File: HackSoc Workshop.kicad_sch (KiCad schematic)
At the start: 35 parts, among them J1 USB_B_Micro, J2 ISP, SW1 SW_Push, SW2 SW_Push, SW3 SW_Push, SW4 SW_Push, SW5 SW_Push, SW6 SW_Push, SW7 SW_Push, U1 ATmega32U4-M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

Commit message: update
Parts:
- SW1, SW2, SW3, SW4, SW5, SW6, SW7: footprint Button_Switch_THT:SW_PUSH_6mm_H8.5mm -> Footprints:SW_TS-1187A-B-A-B
- Y1: footprint Crystal:Crystal_SMD_7050-4Pin_7.0x5.0mm -> Crystal:Crystal_SMD_3225-4Pin_3.2x2.5mm
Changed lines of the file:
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@@
     (property "Reference" "SW1" (id 0) (at 69.215 42.545 0))
     (property "Value" "SW_Push" (id 1) (at 69.215 40.005 0))
-    (property "Footprint" "Button_Switch_THT:SW_PUSH_6mm_H8.5mm" (id 2) (at 69.215 33.655 0)
+    (property "Footprint" "Footprints:SW_TS-1187A-B-A-B" (id 2) (at 69.215 33.655 0)
       (effects (font (size 1.27 1.27)) hide)
     )
@@
     (property "Reference" "SW3" (id 0) (at 117.475 100.965 0))
     (property "Value" "SW_Push" (id 1) (at 132.715 100.965 0))
-    (property "Footprint" "Button_Switch_THT:SW_PUSH_6mm_H8.5mm" (id 2) (at 122.555 97.155 0)
+    (property "Footprint" "Footprints:SW_TS-1187A-B-A-B" (id 2) (at 122.555 97.155 0)
       (effects (font (size 1.27 1.27)) hide)
     )
@@
     (property "Reference" "SW6" (id 0) (at 117.475 108.585 0))
     (property "Value" "SW_Push" (id 1) (at 132.715 108.585 0))
-    (property "Footprint" "Button_Switch_THT:SW_PUSH_6mm_H8.5mm" (id 2) (at 122.555 104.775 0)
+    (property "Footprint" "Footprints:SW_TS-1187A-B-A-B" (id 2) (at 122.555 104.775 0)
       (effects (font (size 1.27 1.27)) hide)
     )
@@
     (property "Reference" "SW2" (id 0) (at 117.475 98.425 0))
     (property "Value" "SW_Push" (id 1) (at 132.715 98.425 0))
-    (property "Footprint" "Button_Switch_THT:SW_PUSH_6mm_H8.5mm" (id 2) (at 122.555 94.615 0)
+    (property "Footprint" "Footprints:SW_TS-1187A-B-A-B" (id 2) (at 122.555 94.615 0)
       (effects (font (size 1.27 1.27)) hide)
     )
@@
     (property "Reference" "SW4" (id 0) (at 117.475 103.505 0))
     (property "Value" "SW_Push" (id 1) (at 132.715 103.505 0))
-    (property "Footprint" "Button_Switch_THT:SW_PUSH_6mm_H8.5mm" (id 2) (at 122.555 99.695 0)
+    (property "Footprint" "Footprints:SW_TS-1187A-B-A-B" (id 2) (at 122.555 99.695 0)
       (effects (font (size 1.27 1.27)) hide)
     )
@@
     (property "Reference" "SW7" (id 0) (at 117.475 111.125 0))
     (property "Value" "SW_Push" (id 1) (at 132.715 111.125 0))
-    (property "Footprint" "Button_Switch_THT:SW_PUSH_6mm_H8.5mm" (id 2) (at 122.555 107.315 0)
+    (property "Footprint" "Footprints:SW_TS-1187A-B-A-B" (id 2) (at 122.555 107.315 0)
       (effects (font (size 1.27 1.27)) hide)
     )
@@
     (property "Reference" "Y1" (id 0) (at 36.195 36.2798 0))
     (property "Value" "12MHz" (id 1) (at 36.195 38.8167 0))
-    (property "Footprint" "Crystal:Crystal_SMD_7050-4Pin_7.0x5.0mm" (id 2) (at 36.195 42.545 0)
+    (property "Footprint" "Crystal:Crystal_SMD_3225-4Pin_3.2x2.5mm" (id 2) (at 36.195 42.545 0)
       (effects (font (size 1.27 1.27)) hide)
     )
@@
     (property "Reference" "SW5" (id 0) (at 117.475 106.045 0))
     (property "Value" "SW_Push" (id 1) (at 132.715 106.045 0))
-    (property "Footprint" "Button_Switch_THT:SW_PUSH_6mm_H8.5mm" (id 2) (at 122.555 102.235 0)
+    (property "Footprint" "Footprints:SW_TS-1187A-B-A-B" (id 2) (at 122.555 102.235 0)
       (effects (font (size 1.27 1.27)) hide)
     )
@@
     )
     (path "/00000000-0000-0000-0000-0000609bc448"
-      (reference "SW1") (unit 1) (value "SW_Push") (footprint "Button_Switch_THT:SW_PUSH_6mm_H8.5mm")
+      (reference "SW1") (unit 1) (value "SW_Push") (footprint "Footprints:SW_TS-1187A-B-A-B")
     )
     (path "/a5cf3bdf-9580-4a89-9b38-de8f920e3709"
-      (reference "SW2") (unit 1) (value "SW_Push") (footprint "Button_Switch_THT:SW_PUSH_6mm_H8.5mm")
+      (reference "SW2") (unit 1) (value "SW_Push") (footprint "Footprints:SW_TS-1187A-B-A-B")
     )
     (path "/1c2ae23d-1cd7-4546-aa49-900e7a3c7475"
-      (reference "SW3") (unit 1) (value "SW_Push") (footprint "Button_Switch_THT:SW_PUSH_6mm_H8.5mm")
+      (reference "SW3") (unit 1) (value "SW_Push") (footprint "Footprints:SW_TS-1187A-B-A-B")
     )
     (path "/e7470108-55db-4f72-aba2-dd70fe36ad14"
-      (reference "SW4") (unit 1) (value "SW_Push") (footprint "Button_Switch_THT:SW_PUSH_6mm_H8.5mm")
+      (reference "SW4") (unit 1) (value "SW_Push") (footprint "Footprints:SW_TS-1187A-B-A-B")
     )
     (path "/fd588f97-a508-46a8-ad7f-2d03d16e0415"
-      (reference "SW5") (unit 1) (value "SW_Push") (footprint "Button_Switch_THT:SW_PUSH_6mm_H8.5mm")
+      (reference "SW5") (unit 1) (value "SW_Push") (footprint "Footprints:SW_TS-1187A-B-A-B")
     )
     (path "/4ad24b1e-891a-4c73-8505-748d30cb04cd"
-      (reference "SW6") (unit 1) (value "SW_Push") (footprint "Button_Switch_THT:SW_PUSH_6mm_H8.5mm")
+      (reference "SW6") (unit 1) (value "SW_Push") (footprint "Footprints:SW_TS-1187A-B-A-B")
     )
     (path "/ea46b088-302a-40e8-b5a2-12e45fa4399e"
-      (reference "SW7") (unit 1) (value "SW_Push") (footprint "Button_Switch_THT:SW_PUSH_6mm_H8.5mm")
+      (reference "SW7") (unit 1) (value "SW_Push") (footprint "Footprints:SW_TS-1187A-B-A-B")
     )
     (path "/b5283b5b-0904-4967-b7ac-90eb3ac0bba7"
@@
     )
     (path "/ef9374d1-0f0d-4d1f-83b4-60e96f215708"
-      (reference "Y1") (unit 1) (value "12MHz") (footprint "Crystal:Crystal_SMD_7050-4Pin_7.0x5.0mm")
-    )
-  )
+      (reference "Y1") (unit 1) (value "12MHz") (footprint "Crystal:Crystal_SMD_3225-4Pin_3.2x2.5mm")
+    )
+  )

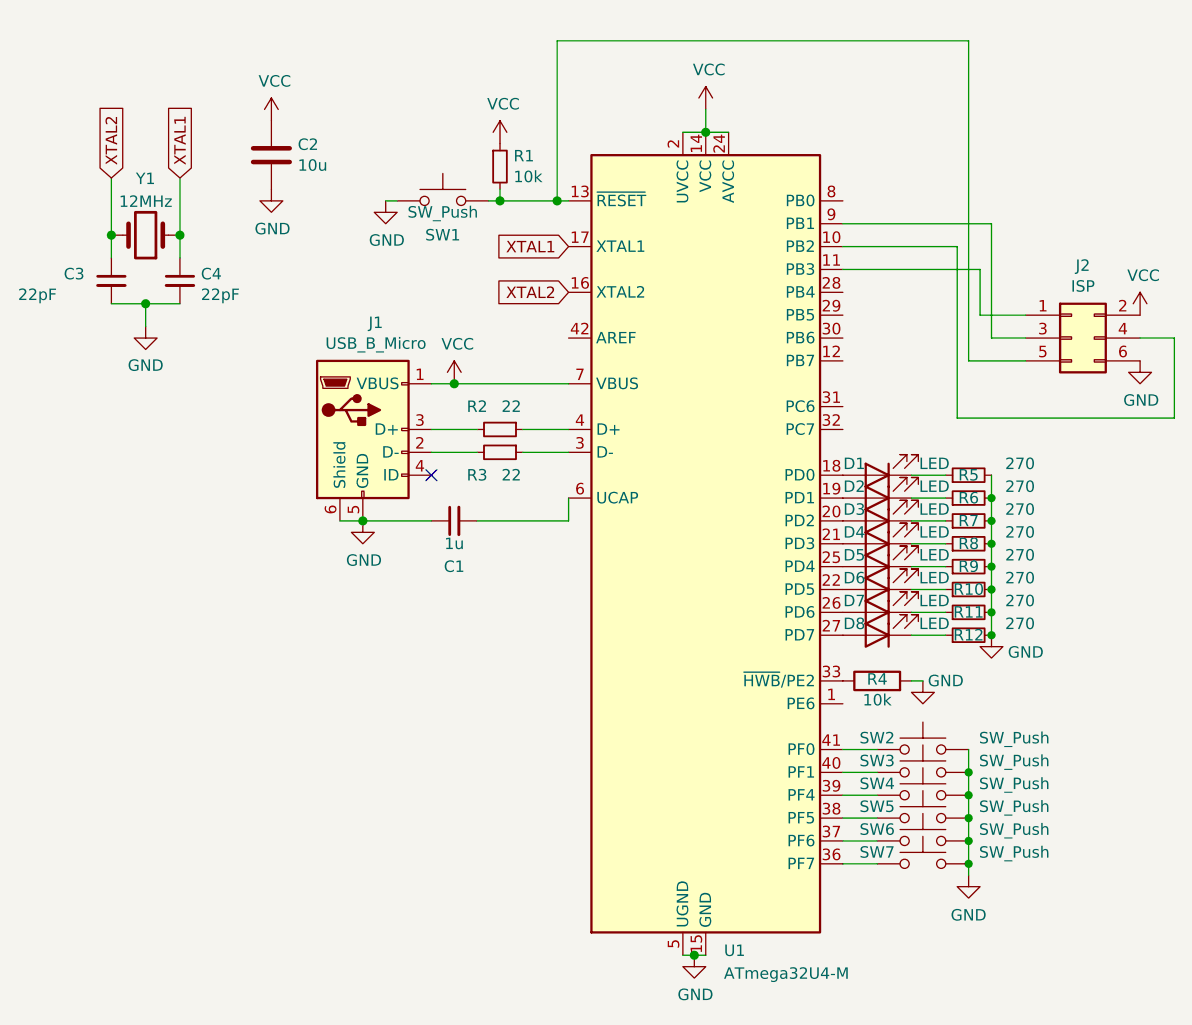
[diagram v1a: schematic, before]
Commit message: remove pcb
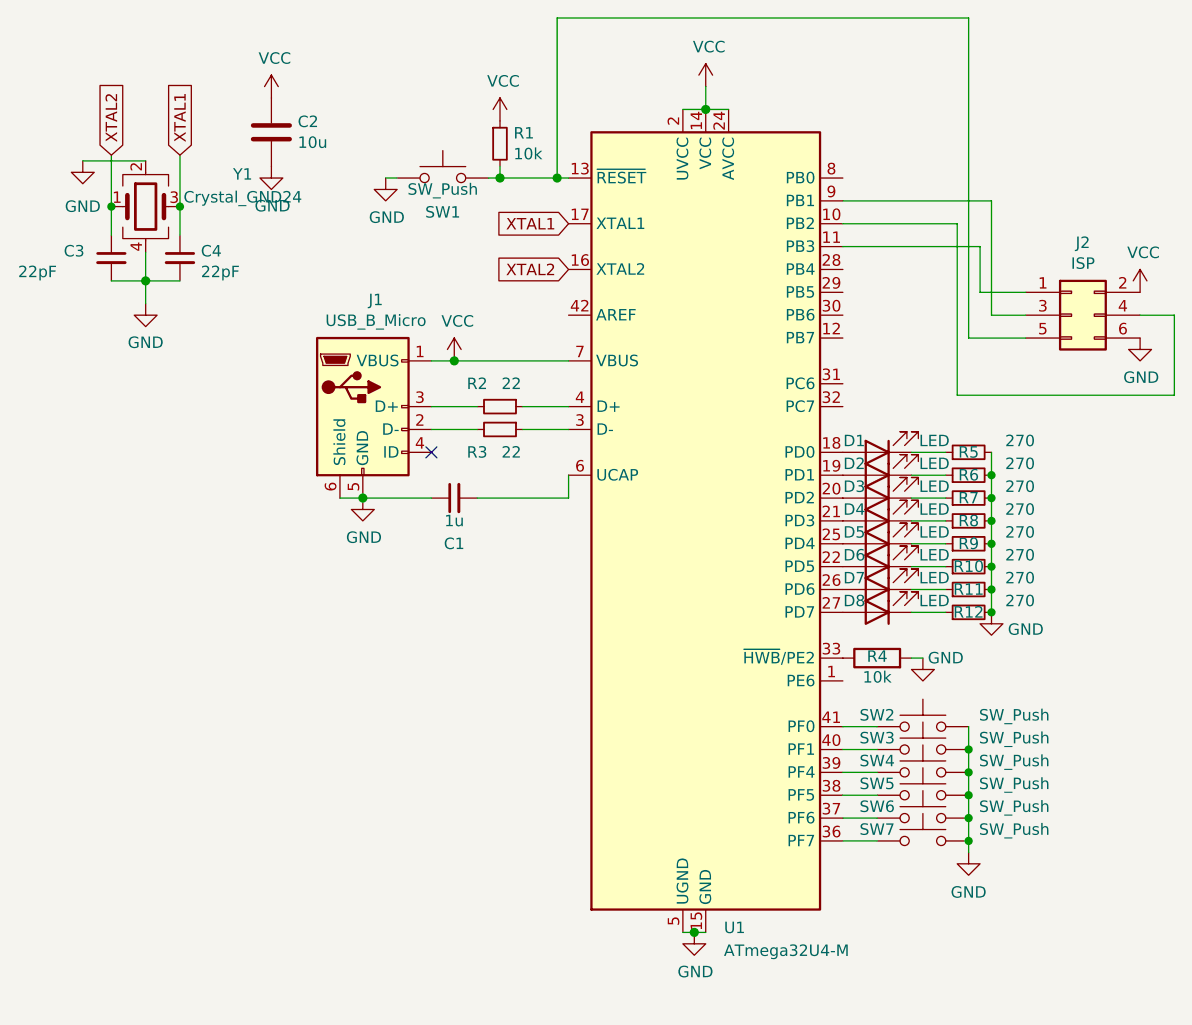
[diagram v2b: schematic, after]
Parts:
- removed Y1: 12MHz, Crystal:Crystal_SMD_3225-4Pin_3.2x2.5mm, symbol Device:Crystal
- added Y1: Crystal_GND24, Crystal:Crystal_SMD_3225-4Pin_3.2x2.5mm, symbol Device:Crystal_GND24
- SW1, SW2, SW3, SW4, SW5, SW6, SW7: footprint Footprints:SW_TS-1187A-B-A-B -> Button_Switch_THT:SW_PUSH_6mm_H8.5mm
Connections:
- net GND: now also Y1.2, Y1.4
- net XTAL1: now also Y1.3
- net XTAL2: now also Y1.1
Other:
- moved on the sheet: C1, C2, C3, C4, D1, D2, D3, D4, D5, D6, D7, D8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
